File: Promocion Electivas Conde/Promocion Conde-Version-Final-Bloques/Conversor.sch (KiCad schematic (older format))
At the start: 0 parts

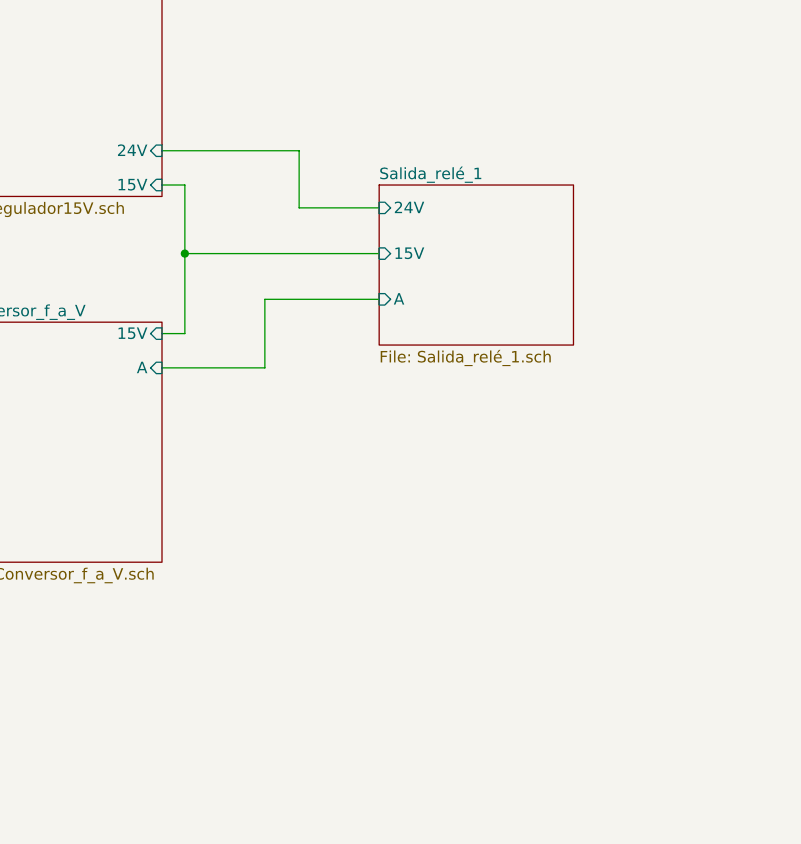
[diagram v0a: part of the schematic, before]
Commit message: Agregue circuito 4-20 mA a la version en bloques
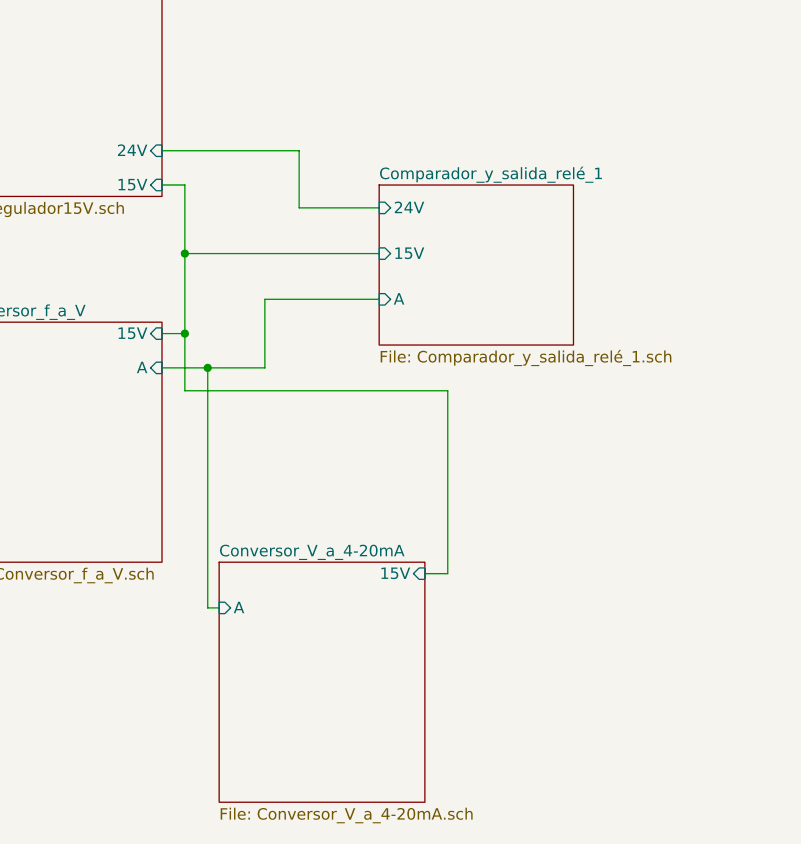
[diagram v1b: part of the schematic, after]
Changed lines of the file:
@@
 $Descr A4 11693 8268
 encoding utf-8
-Sheet 1 4
+Sheet 1 5
 Title ""
 Date ""
@@
 S 3900 2150 850  700
 U 61322896
-F0 "Salida_relé_1" 50
-F1 "Salida_relé_1.sch" 50
+F0 "Comparador_y_salida_relé_1" 50
+F1 "Comparador_y_salida_relé_1.sch" 50
 F2 "A" I L 3900 2650 50
 F3 "15V" I L 3900 2450 50
@@
 	3050 2150 2950 2150
 Wire Wire Line
-	2950 2950 3400 2950
+	2950 2950 3150 2950
 Wire Wire Line
 	3400 2950 3400 2650
@@
 Wire Wire Line
 	3550 2000 2950 2000
+Wire Wire Line
+	4100 3850 4200 3850
+$Sheet
+S 3200 3800 900  1050
+U 6184FF73
+F0 "Conversor_V_a_4-20mA" 50
+F1 "Conversor_V_a_4-20mA.sch" 50
+F2 "A" I L 3200 4000 50
+F3 "15V" I R 4100 3850 50
+$EndSheet
+Wire Wire Line
+	4200 3850 4200 3050
+Wire Wire Line
+	4200 3050 3050 3050
+Wire Wire Line
+	3050 3050 3050 2800
+Connection ~ 3050 2800
+Wire Wire Line
+	3200 4000 3150 4000
+Wire Wire Line
+	3150 4000 3150 2950
+Connection ~ 3150 2950
+Wire Wire Line
+	3150 2950 3400 2950
 $EndSCHEMATC

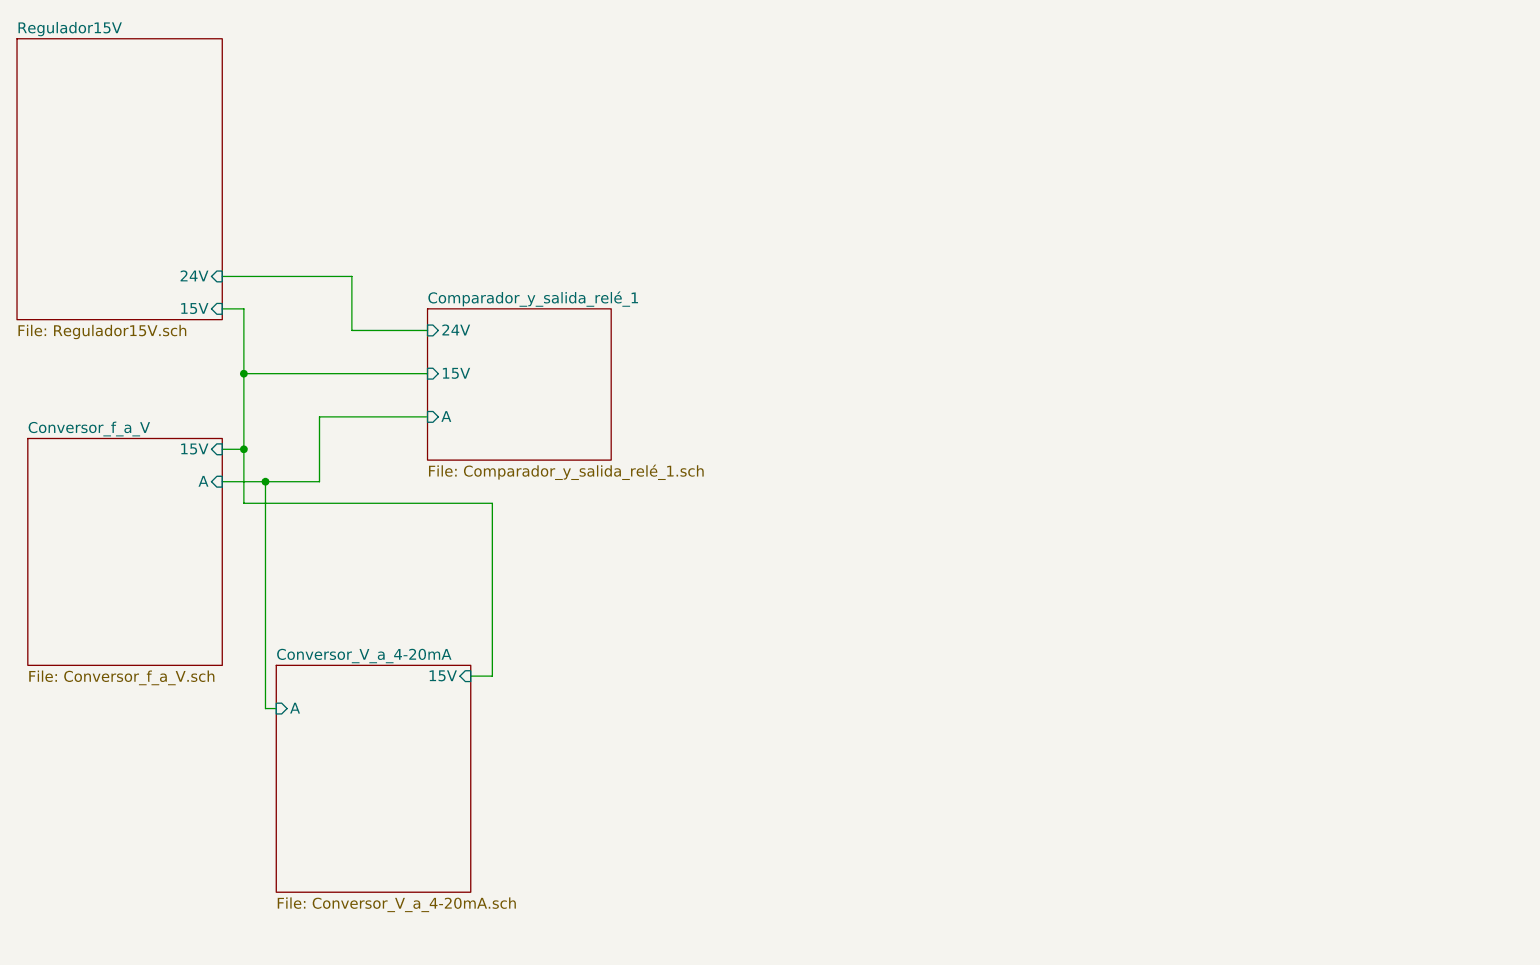
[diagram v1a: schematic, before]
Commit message: Bloques y footprint asignados
Falta elegir y asignar el de los potenciometros Rv3 y Rv7.
Las salidas K3 y K20 también...
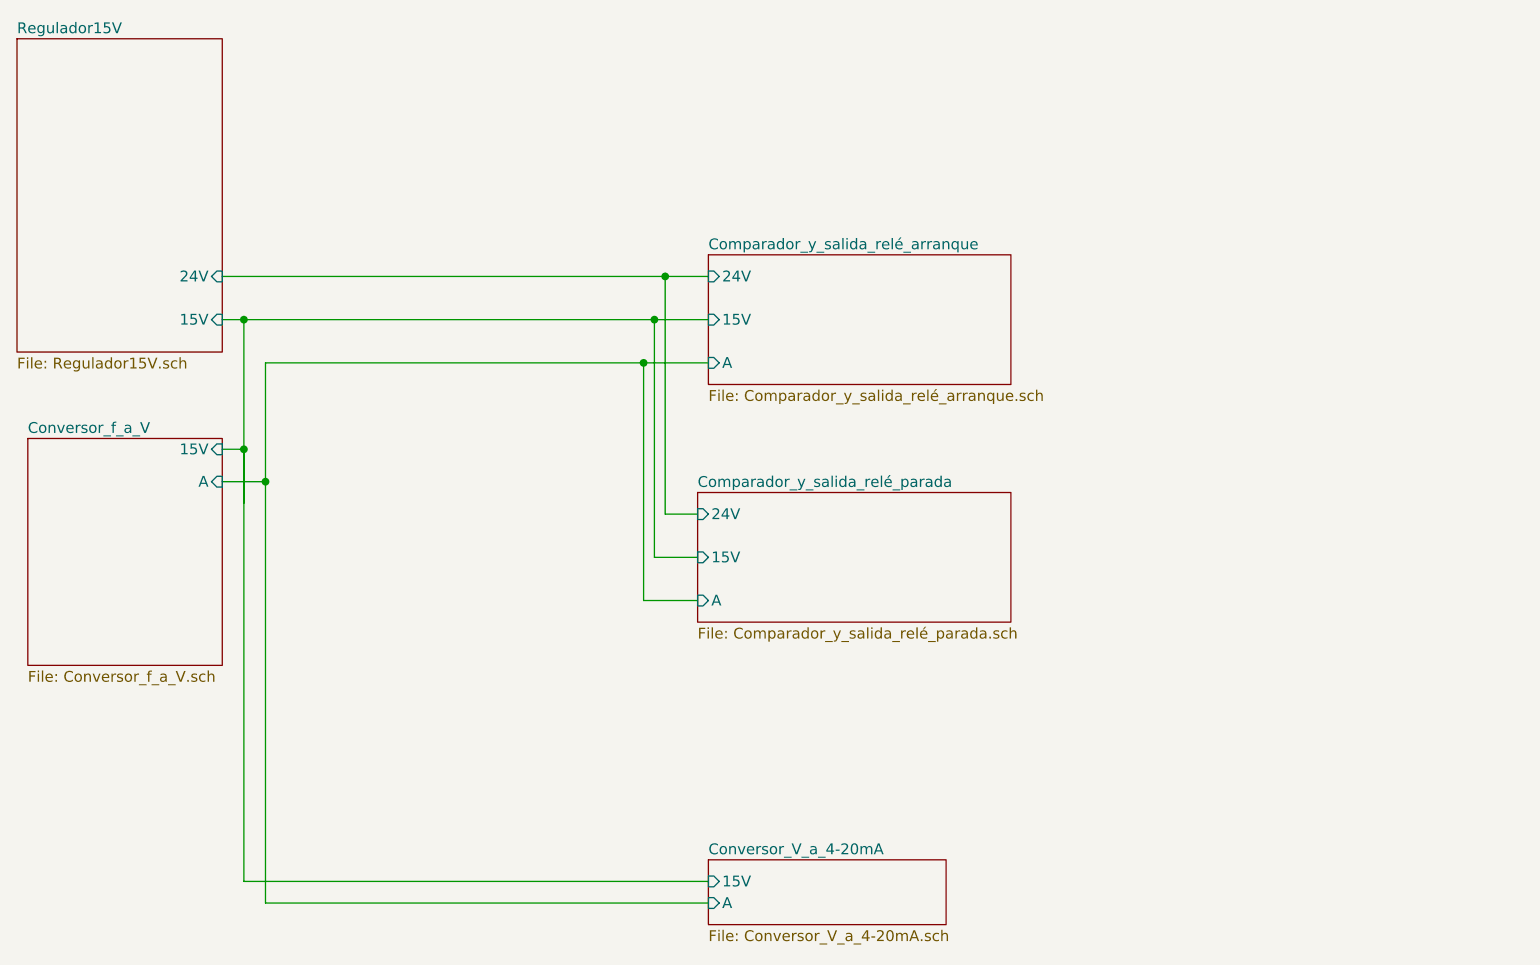
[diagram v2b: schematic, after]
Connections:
- wire segments 18 -> 22
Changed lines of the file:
@@
 $Descr A4 11693 8268
 encoding utf-8
-Sheet 1 5
+Sheet 1 6
 Title ""
 Date ""
@@
 F3 "15V" I R 2950 2800 50
 $EndSheet
+Wire Wire Line
+	2950 2800 3050 2800
+Wire Wire Line
+	2950 2950 3150 2950
 $Sheet
-S 2000 900  950  1300
+S 5200 4700 1100 300
+U 6184FF73
+F0 "Conversor_V_a_4-20mA" 50
+F1 "Conversor_V_a_4-20mA.sch" 50
+F2 "A" I L 5200 4900 50
+F3 "15V" I L 5200 4800 50
+$EndSheet
+$Sheet
+S 5200 1900 1400 600
+U 61322896
+F0 "Comparador_y_salida_relé_arranque" 50
+F1 "Comparador_y_salida_relé_arranque.sch" 50
+F2 "A" I L 5200 2400 50
+F3 "15V" I L 5200 2200 50
+F4 "24V" I L 5200 2000 50
+$EndSheet
+Wire Wire Line
+	5200 2200 4950 2200
+$Sheet
+S 5150 3000 1450 600
+U 618B375A
+F0 "Comparador_y_salida_relé_parada" 50
+F1 "Comparador_y_salida_relé_parada.sch" 50
+F2 "A" I L 5150 3500 50
+F3 "15V" I L 5150 3300 50
+F4 "24V" I L 5150 3100 50
+$EndSheet
+Wire Wire Line
+	2950 2000 5000 2000
+Wire Wire Line
+	5150 3100 5000 3100
+Wire Wire Line
+	5000 3100 5000 2000
+Connection ~ 5000 2000
+Wire Wire Line
+	5000 2000 5200 2000
+Wire Wire Line
+	5150 3300 4950 3300
+Wire Wire Line
+	4950 3300 4950 2200
+Connection ~ 4950 2200
+Wire Wire Line
+	5150 3500 4900 3500
+Wire Wire Line
+	4900 3500 4900 2400
+Connection ~ 4900 2400
+Wire Wire Line
+	4900 2400 5200 2400
+$Sheet
+S 2000 900  950  1450
 U 612E3FD7
 F0 "Regulador15V" 50
 F1 "Regulador15V.sch" 50
-F2 "15V" I R 2950 2150 50
+F2 "15V" I R 2950 2200 50
 F3 "24V" I R 2950 2000 50
 $EndSheet
-$Sheet
-S 3900 2150 850  700
-U 61322896
-F0 "Comparador_y_salida_relé_1" 50
-F1 "Comparador_y_salida_relé_1.sch" 50
-F2 "A" I L 3900 2650 50
-F3 "15V" I L 3900 2450 50
-F4 "24V" I L 3900 2250 50
-$EndSheet
 Wire Wire Line
-	2950 2800 3050 2800
+	2950 2200 3050 2200
 Wire Wire Line
-	3050 2800 3050 2450
+	3050 2800 3050 2200
+Connection ~ 3050 2800
+Connection ~ 3050 2200
 Wire Wire Line
-	3050 2150 2950 2150
+	3050 2200 4950 2200
 Wire Wire Line
-	2950 2950 3150 2950
+	3150 2400 3150 2950
 Wire Wire Line
-	3400 2950 3400 2650
+	3150 2400 4900 2400
 Wire Wire Line
-	3400 2650 3900 2650
+	3150 4900 3150 2950
 Wire Wire Line
-	3900 2450 3050 2450
-Connection ~ 3050 2450
+	3150 4900 5200 4900
+Connection ~ 3150 2950
 Wire Wire Line
-	3050 2450 3050 2150
-Wire Wire Line
-	3900 2250 3550 2250
-Wire Wire Line
-	3550 2250 3550 2000
-Wire Wire Line
-	3550 2000 2950 2000
-Wire Wire Line
-	4100 3850 4200 3850
-$Sheet
-S 3200 3800 900  1050
-U 6184FF73
-F0 "Conversor_V_a_4-20mA" 50
-F1 "Conversor_V_a_4-20mA.sch" 50
-F2 "A" I L 3200 4000 50
-F3 "15V" I R 4100 3850 50
-$EndSheet
-Wire Wire Line
-	4200 3850 4200 3050
-Wire Wire Line
-	4200 3050 3050 3050
+	5200 4800 3050 4800
 Wire Wire Line
 	3050 3050 3050 2800
-Connection ~ 3050 2800
 Wire Wire Line
-	3200 4000 3150 4000
-Wire Wire Line
-	3150 4000 3150 2950
-Connection ~ 3150 2950
-Wire Wire Line
-	3150 2950 3400 2950
+	3050 2800 3050 4800
 $EndSCHEMATC

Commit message: Actualizacion Convertidor
Se creó el esquemático del convertidor y se hizo la conexión del mismo
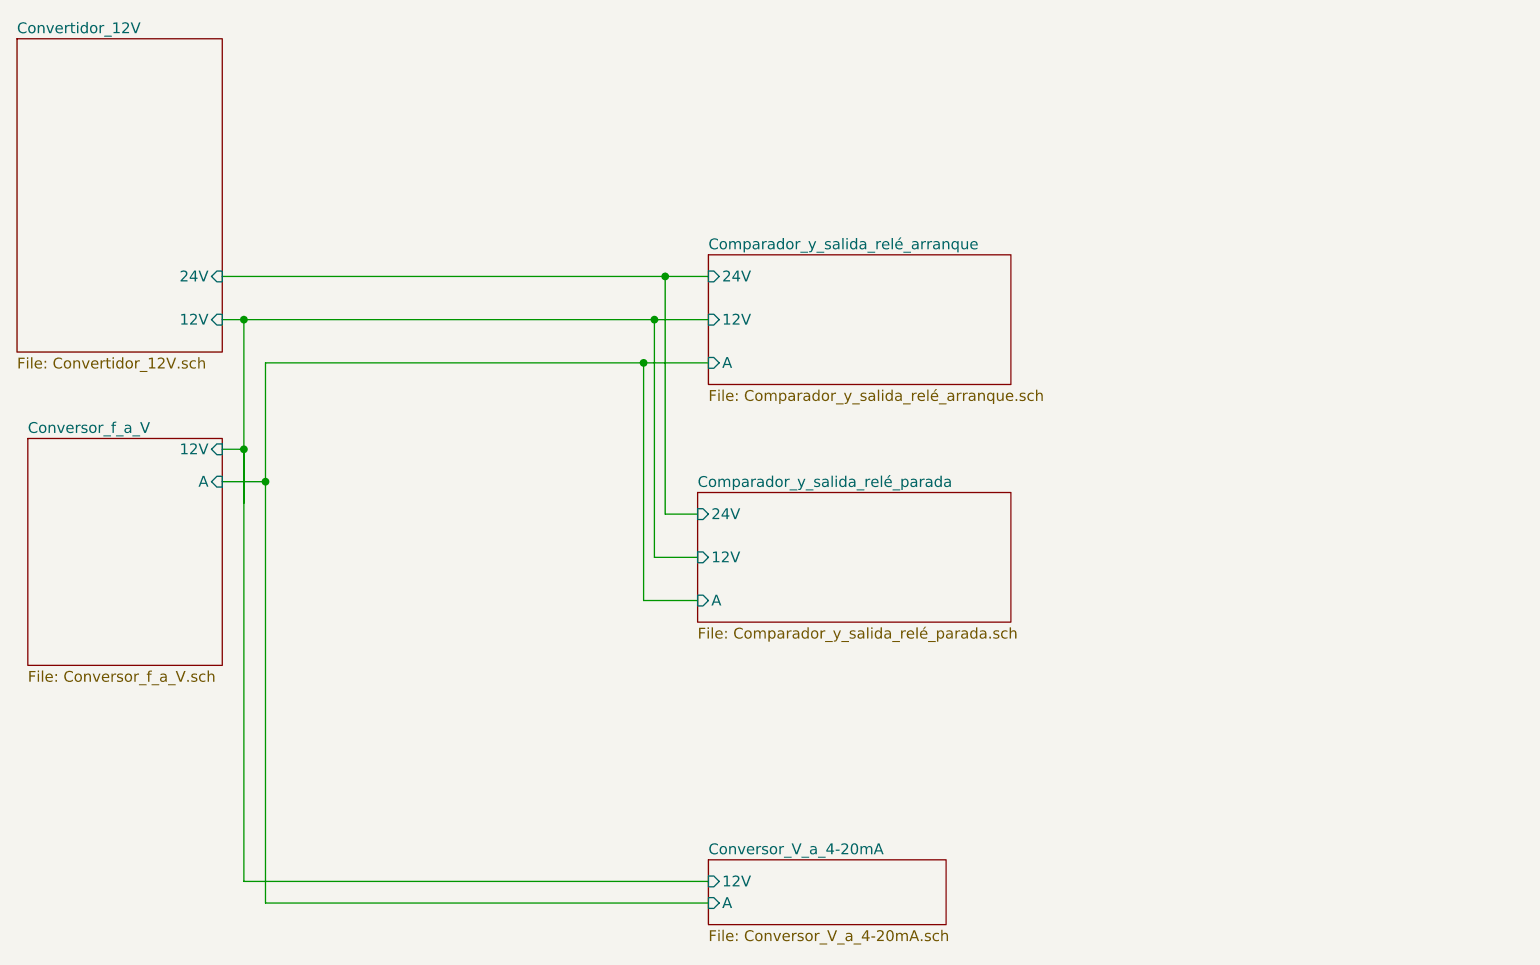
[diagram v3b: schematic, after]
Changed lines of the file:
@@
 F1 "Conversor_f_a_V.sch" 50
 F2 "A" I R 2950 2950 50
-F3 "15V" I R 2950 2800 50
+F3 "12V" I R 2950 2800 50
 $EndSheet
 Wire Wire Line
@@
 F1 "Conversor_V_a_4-20mA.sch" 50
 F2 "A" I L 5200 4900 50
-F3 "15V" I L 5200 4800 50
+F3 "12V" I L 5200 4800 50
 $EndSheet
 $Sheet
@@
 F1 "Comparador_y_salida_relé_arranque.sch" 50
 F2 "A" I L 5200 2400 50
-F3 "15V" I L 5200 2200 50
+F3 "12V" I L 5200 2200 50
 F4 "24V" I L 5200 2000 50
 $EndSheet
@@
 F1 "Comparador_y_salida_relé_parada.sch" 50
 F2 "A" I L 5150 3500 50
-F3 "15V" I L 5150 3300 50
+F3 "12V" I L 5150 3300 50
 F4 "24V" I L 5150 3100 50
 $EndSheet
@@
 Wire Wire Line
 	4900 2400 5200 2400
-$Sheet
-S 2000 900  950  1450
-U 612E3FD7
-F0 "Regulador15V" 50
-F1 "Regulador15V.sch" 50
-F2 "15V" I R 2950 2200 50
-F3 "24V" I R 2950 2000 50
-$EndSheet
 Wire Wire Line
 	2950 2200 3050 2200
@@
 Wire Wire Line
 	3050 2800 3050 4800
+$Sheet
+S 2000 900  950  1450
+U 612E3FD7
+F0 "Convertidor_12V" 50
+F1 "Convertidor_12V.sch" 50
+F2 "12V" I R 2950 2200 50
+F3 "24V" I R 2950 2000 50
+$EndSheet
 $EndSCHEMATC

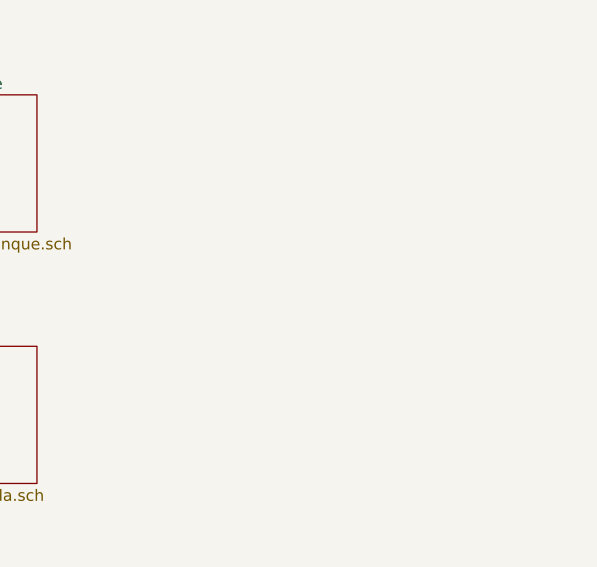
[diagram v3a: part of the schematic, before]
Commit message: Actualizacion
Actualizo los footprints del esquematico y se inicia el PCB
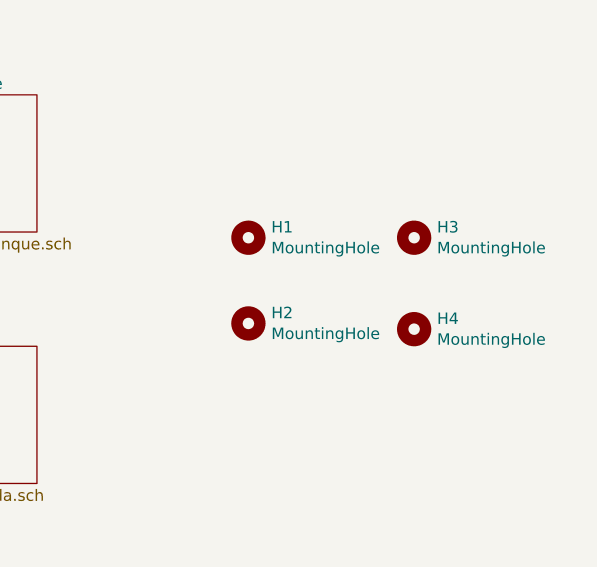
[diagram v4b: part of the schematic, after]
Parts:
- added H1, H2, H3, H4: MountingHole, MountingHole:MountingHole_3.2mm_M3, symbol Mechanical:MountingHole
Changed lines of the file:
@@
 F3 "24V" I R 2950 2000 50
 $EndSheet
+$Comp
+L Mechanical:MountingHole H1
+U 1 1 6194C4E5
+P 7525 2525
+F 0 "H1" H 7625 2571 50  0000 L CNN
+F 1 "MountingHole" H 7625 2480 50  0000 L CNN
+F 2 "MountingHole:MountingHole_3.2mm_M3" H 7525 2525 50  0001 C CNN
+F 3 "~" H 7525 2525 50  0001 C CNN
+	1    7525 2525
+	1    0    0    -1
+$EndComp
+$Comp
+L Mechanical:MountingHole H3
+U 1 1 6194D0A7
+P 8250 2525
+F 0 "H3" H 8350 2571 50  0000 L CNN
+F 1 "MountingHole" H 8350 2480 50  0000 L CNN
+F 2 "MountingHole:MountingHole_3.2mm_M3" H 8250 2525 50  0001 C CNN
+F 3 "~" H 8250 2525 50  0001 C CNN
+	1    8250 2525
+	1    0    0    -1
+$EndComp
+$Comp
+L Mechanical:MountingHole H2
+U 1 1 6194D435
+P 7525 2900
+F 0 "H2" H 7625 2946 50  0000 L CNN
+F 1 "MountingHole" H 7625 2855 50  0000 L CNN
+F 2 "MountingHole:MountingHole_3.2mm_M3" H 7525 2900 50  0001 C CNN
+F 3 "~" H 7525 2900 50  0001 C CNN
+	1    7525 2900
+	1    0    0    -1
+$EndComp
+$Comp
+L Mechanical:MountingHole H4
+U 1 1 6194D618
+P 8250 2925
+F 0 "H4" H 8350 2971 50  0000 L CNN
+F 1 "MountingHole" H 8350 2880 50  0000 L CNN
+F 2 "MountingHole:MountingHole_3.2mm_M3" H 8250 2925 50  0001 C CNN
+F 3 "~" H 8250 2925 50  0001 C CNN
+	1    8250 2925
+	1    0    0    -1
+$EndComp
 $EndSCHEMATC
